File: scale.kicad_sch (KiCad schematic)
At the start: 10 parts, among them J1 Conn_01x02_Pin, J2 Conn_01x04_Pin, J4 Conn_01x05_Pin

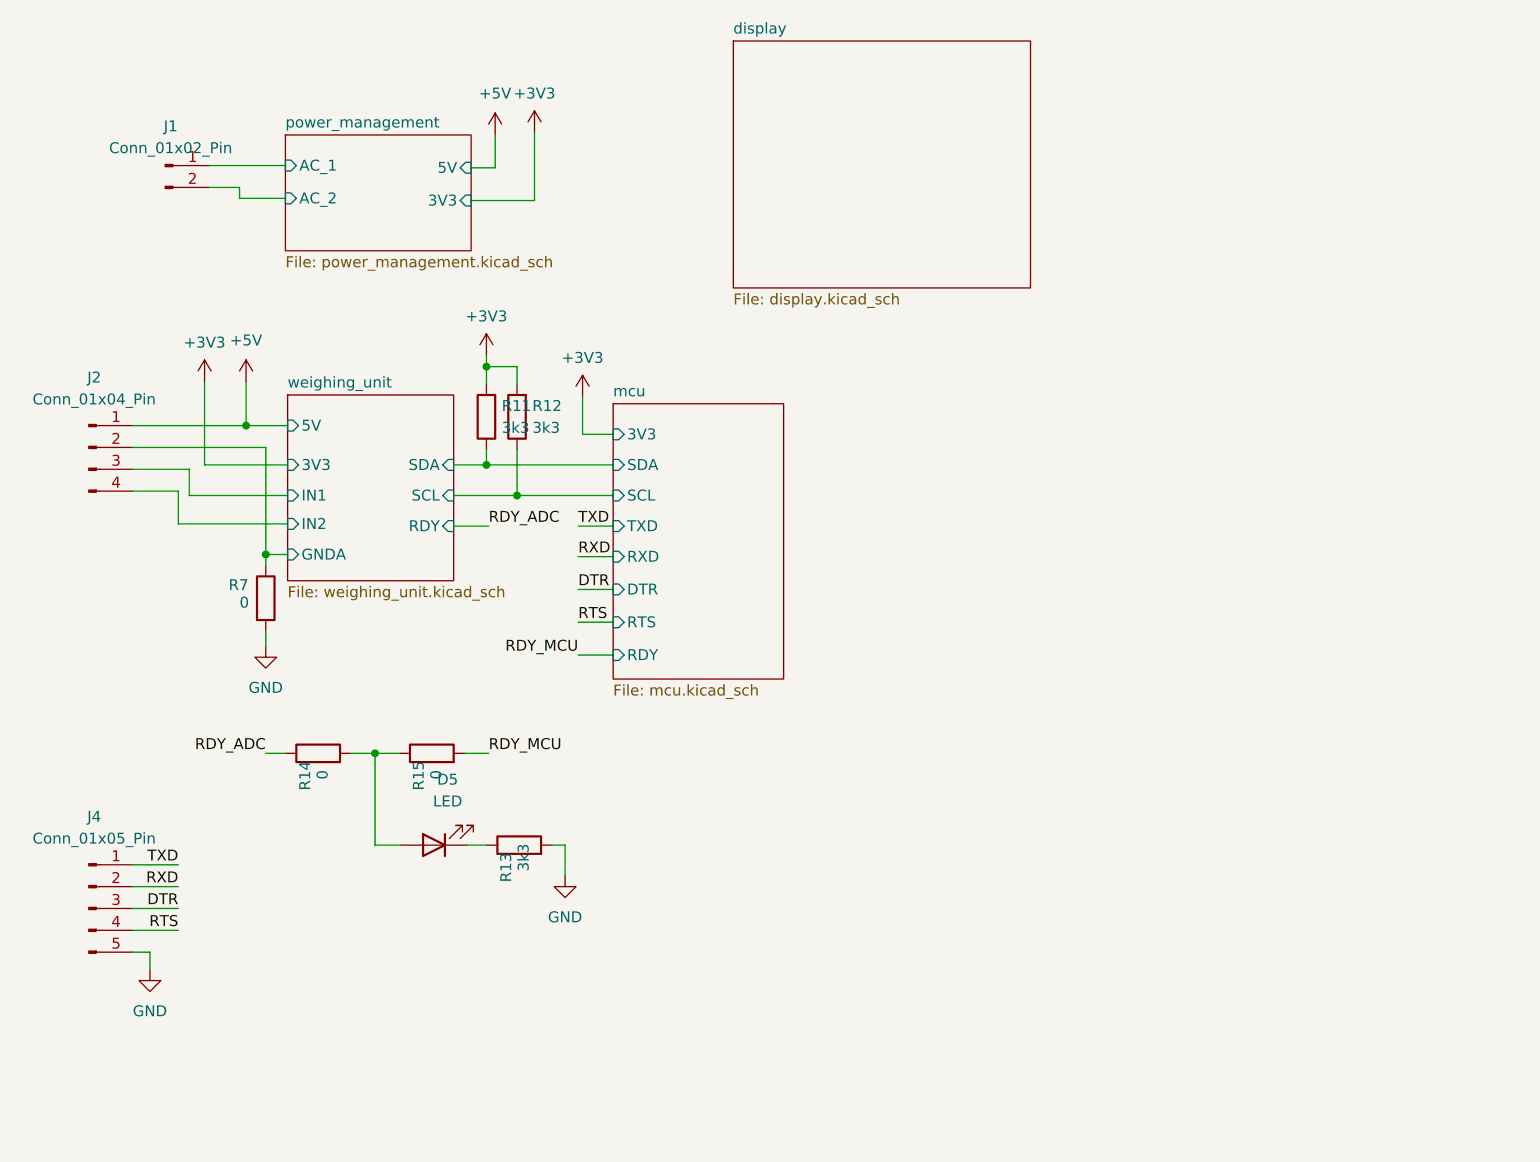
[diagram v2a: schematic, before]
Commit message: add footprint and step
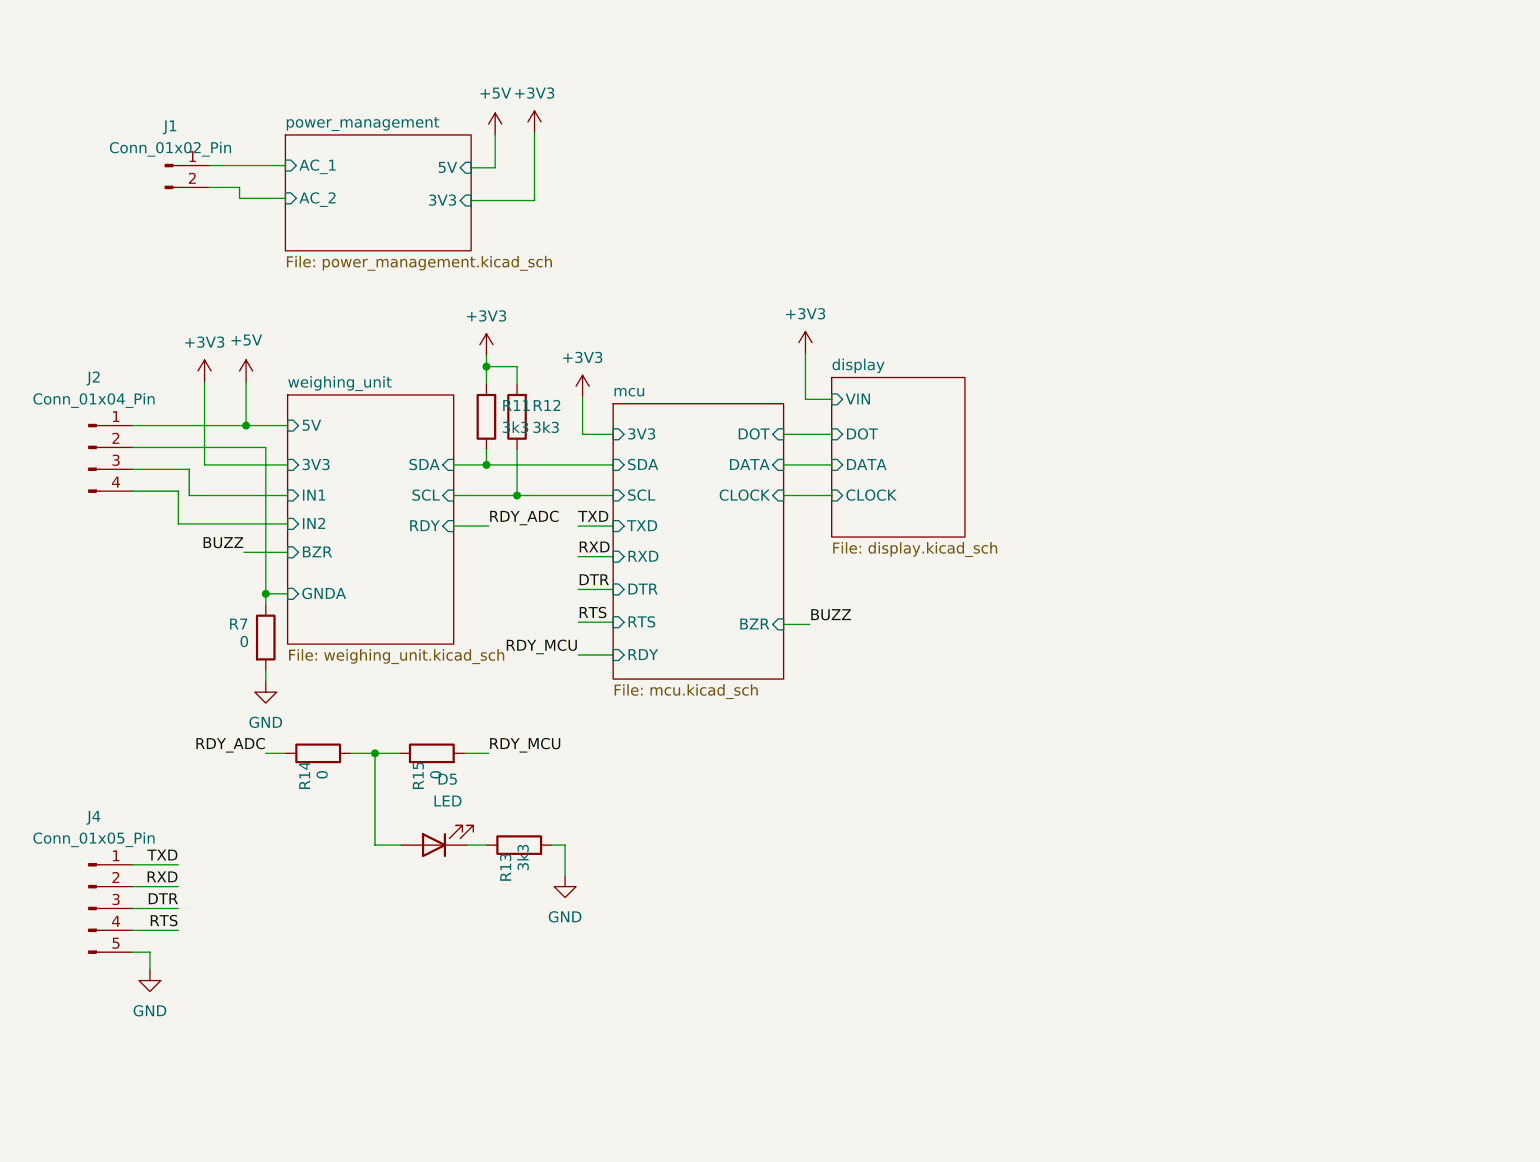
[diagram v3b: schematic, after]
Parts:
- J1: footprint (none) -> BBG:CONN2_284513-2
- J2: footprint (none) -> BBG:JST_S4B-XH-A(LF)(SN)
- J4: footprint (none) -> Connector_PinHeader_2.54mm:PinHeader_1x05_P2.54mm_Vertical
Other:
- sheet display ports: added CLOCK, DATA, DOT, VIN; removed none
- sheet mcu ports: added BZR, CLOCK, DATA, DOT; removed none
- sheet weighing_unit ports: added BZR; removed none
- moved on the sheet: R7
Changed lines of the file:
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@@
   (junction (at 41.402 77.978) (diameter 0) (color 0 0 0 0)
   )
-  (junction (at 43.688 92.964) (diameter 0) (color 0 0 0 0)
-  )
-  (wire (pts (xy 46.228 92.964) (xy 43.688 92.964))
+  (junction (at 43.688 97.536) (diameter 0) (color 0 0 0 0)
+  )
+  (wire (pts (xy 46.228 97.536) (xy 43.688 97.536))
     (stroke (width 0) (type default))
   )
@@
     (stroke (width 0) (type default))
   )
-  (wire (pts (xy 43.688 80.518) (xy 43.688 92.964))
-    (stroke (width 0) (type default))
-  )
   (wire (pts (xy 34.798 83.058) (xy 28.194 83.058))
     (stroke (width 0) (type default))
@@
     (stroke (width 0) (type default))
   )
+  (wire (pts (xy 103.886 78.994) (xy 109.474 78.994))
+    (stroke (width 0) (type default))
+  )
   (wire (pts (xy 36.576 72.898) (xy 36.576 82.55))
     (stroke (width 0) (type default))
@@
     (stroke (width 0) (type default))
   )
+  (wire (pts (xy 103.886 86.106) (xy 109.474 86.106))
+    (stroke (width 0) (type default))
+  )
   (wire (pts (xy 46.228 86.106) (xy 34.798 86.106))
     (stroke (width 0) (type default))
@@
     (stroke (width 0) (type default))
   )
-  (wire (pts (xy 43.688 92.964) (xy 43.688 94.234))
+  (wire (pts (xy 43.688 80.518) (xy 43.688 97.536))
     (stroke (width 0) (type default))
   )
@@
     (stroke (width 0) (type default))
   )
+  (wire (pts (xy 103.886 82.55) (xy 109.474 82.55))
+    (stroke (width 0) (type default))
+  )
   (wire (pts (xy 40.64 50.292) (xy 37.084 50.292))
     (stroke (width 0) (type default))
@@
     (stroke (width 0) (type default))
   )
+  (wire (pts (xy 41.148 92.71) (xy 46.228 92.71))
+    (stroke (width 0) (type default))
+  )
+  (wire (pts (xy 43.688 97.536) (xy 43.688 98.806))
+    (stroke (width 0) (type default))
+  )
   (wire (pts (xy 67.564 48.006) (xy 70.358 48.006))
     (stroke (width 0) (type default))
@@
     (stroke (width 0) (type default))
   )
-  (wire (pts (xy 43.688 101.854) (xy 43.688 103.632))
+  (wire (pts (xy 103.886 101.092) (xy 106.934 101.092))
+    (stroke (width 0) (type default))
+  )
+  (wire (pts (xy 43.688 106.426) (xy 43.688 107.696))
     (stroke (width 0) (type default))
   )
@@
     (stroke (width 0) (type default))
   )
+  (wire (pts (xy 106.426 74.93) (xy 106.426 69.596))
+    (stroke (width 0) (type default))
+  )
   (wire (pts (xy 28.194 129.032) (xy 33.528 129.032))
     (stroke (width 0) (type default))
@@
   )
   (wire (pts (xy 43.688 116.078) (xy 45.974 116.078))
+    (stroke (width 0) (type default))
+  )
+  (wire (pts (xy 109.474 74.93) (xy 106.426 74.93))
     (stroke (width 0) (type default))
   )
@@
     (effects (font (size 1.27 1.27)) (justify left bottom))
   )
+  (label "BUZZ" (at 41.148 92.71 180) (fields_autoplaced)
+    (effects (font (size 1.27 1.27)) (justify right bottom))
+  )
+  (label "BUZZ" (at 106.934 101.092 0) (fields_autoplaced)
+    (effects (font (size 1.27 1.27)) (justify left bottom))
+  )
   (symbol (lib_id "power:+5V") (at 41.402 72.898 0) (unit 1)
     (in_bom yes) (on_board yes) (dnp no) (fields_autoplaced)
@@
       (effects (font (size 1.27 1.27)))
     )
-    (property "Footprint" "" (at 23.114 80.518 0)
+    (property "Footprint" "BBG:JST_S4B-XH-A(LF)(SN)" (at 23.114 80.518 0)
       (effects (font (size 1.27 1.27)) hide)
     )
@@
       (effects (font (size 1.27 1.27)))
     )
-    (property "Footprint" "" (at 32.004 47.752 0)
+    (property "Footprint" "BBG:CONN2_284513-2" (at 32.004 47.752 0)
       (effects (font (size 1.27 1.27)) hide)
     )
@@
     )
   )
-  (symbol (lib_id "power:GND") (at 43.688 103.632 0) (unit 1)
-    (in_bom yes) (on_board yes) (dnp no) (fields_autoplaced)
-    (property "Reference" "#PWR016" (at 43.688 109.982 0)
-      (effects (font (size 1.27 1.27)) hide)
-    )
-    (property "Value" "GND" (at 43.688 108.458 0)
-      (effects (font (size 1.27 1.27)))
-    )
-    (property "Footprint" "" (at 43.688 103.632 0)
-      (effects (font (size 1.27 1.27)) hide)
-    )
-    (property "Datasheet" "" (at 43.688 103.632 0)
+  (symbol (lib_id "power:GND") (at 43.688 107.696 0) (unit 1)
+    (in_bom yes) (on_board yes) (dnp no) (fields_autoplaced)
+    (property "Reference" "#PWR016" (at 43.688 114.046 0)
+      (effects (font (size 1.27 1.27)) hide)
+    )
+    (property "Value" "GND" (at 43.688 112.522 0)
+      (effects (font (size 1.27 1.27)))
+    )
+    (property "Footprint" "" (at 43.688 107.696 0)
+      (effects (font (size 1.27 1.27)) hide)
+    )
+    (property "Datasheet" "" (at 43.688 107.696 0)
       (effects (font (size 1.27 1.27)) hide)
     )
@@
       (effects (font (size 1.27 1.27)))
     )
-    (property "Footprint" "" (at 23.114 134.112 0)
+    (property "Footprint" "Connector_PinHeader_2.54mm:PinHeader_1x05_P2.54mm_Vertical" (at 23.114 134.112 0)
       (effects (font (size 1.27 1.27)) hide)
     )
@@
     )
   )
+  (symbol (lib_id "power:+3V3") (at 106.426 69.596 0) (unit 1)
+    (in_bom yes) (on_board yes) (dnp no) (fields_autoplaced)
+    (property "Reference" "#PWR031" (at 106.426 73.406 0)
+      (effects (font (size 1.27 1.27)) hide)
+    )
+    (property "Value" "+3V3" (at 106.426 65.024 0)
+      (effects (font (size 1.27 1.27)))
+    )
+    (property "Footprint" "" (at 106.426 69.596 0)
+      (effects (font (size 1.27 1.27)) hide)
+    )
+    (property "Datasheet" "" (at 106.426 69.596 0)
+      (effects (font (size 1.27 1.27)) hide)
+    )
+    (pin "1")
+    (instances
+      (project "scale"
+        (path "/8f227bf3-f4cf-485c-a746-8377af835d89"
+          (reference "#PWR031") (unit 1)
+        )
+      )
+    )
+  )
   (symbol (lib_id "Device:R") (at 49.784 116.078 90) (unit 1)
     (in_bom yes) (on_board yes) (dnp no)
@@
     )
   )
-  (symbol (lib_id "Device:R") (at 43.688 98.044 0) (unit 1)
+  (symbol (lib_id "Device:R") (at 43.688 102.616 0) (unit 1)
     (in_bom yes) (on_board yes) (dnp no)
-    (property "Reference" "R7" (at 39.37 96.52 0)
-      (effects (font (size 1.27 1.27)) (justify left))
-    )
-    (property "Value" "0" (at 40.64 98.552 0)
-      (effects (font (size 1.27 1.27)) (justify left))
-    )
-    (property "Footprint" "Resistor_SMD:R_0805_2012Metric" (at 41.91 98.044 90)
-      (effects (font (size 1.27 1.27)) hide)
-    )
-    (property "Datasheet" "~" (at 43.688 98.044 0)
+    (property "Reference" "R7" (at 39.37 101.092 0)
+      (effects (font (size 1.27 1.27)) (justify left))
+    )
+    (property "Value" "0" (at 40.64 103.124 0)
+      (effects (font (size 1.27 1.27)) (justify left))
+    )
+    (property "Footprint" "Resistor_SMD:R_0805_2012Metric" (at 41.91 102.616 90)
+      (effects (font (size 1.27 1.27)) hide)
+    )
+    (property "Datasheet" "~" (at 43.688 102.616 0)
       (effects (font (size 1.27 1.27)) hide)
     )
@@
       (effects (font (size 1.27 1.27)) (justify left))
     )
+    (pin "DOT" input (at 103.886 78.994 0)
+      (effects (font (size 1.27 1.27)) (justify right))
+    )
+    (pin "DATA" input (at 103.886 82.55 0)
+      (effects (font (size 1.27 1.27)) (justify right))
+    )
+    (pin "CLOCK" input (at 103.886 86.106 0)
+      (effects (font (size 1.27 1.27)) (justify right))
+    )
+    (pin "BZR" input (at 103.886 101.092 0)
+      (effects (font (size 1.27 1.27)) (justify right))
+    )
     (instances
       (project "scale"
@@
     )
   )
-  (sheet (at 46.228 74.422) (size 19.304 21.59) (fields_autoplaced)
+  (sheet (at 46.228 74.422) (size 19.304 28.956) (fields_autoplaced)
     (stroke (width 0.1524) (type solid))
     (fill (color 0 0 0 0.0000))
@@
       (effects (font (size 1.27 1.27)) (justify left bottom))
     )
-    (property "Sheetfile" "weighing_unit.kicad_sch" (at 46.228 96.5966 0)
+    (property "Sheetfile" "weighing_unit.kicad_sch" (at 46.228 103.9626 0)
       (effects (font (size 1.27 1.27)) (justify left top))
     )
@@
       (effects (font (size 1.27 1.27)) (justify left))
     )
-    (pin "GNDA" input (at 46.228 92.964 180)
+    (pin "GNDA" input (at 46.228 97.536 180)
       (effects (font (size 1.27 1.27)) (justify left))
     )
@@
     (pin "SDA" input (at 65.532 82.55 0)
       (effects (font (size 1.27 1.27)) (justify right))
+    )
+    (pin "BZR" input (at 46.228 92.71 180)
+      (effects (font (size 1.27 1.27)) (justify left))
     )
     (instances
@@
     )
   )
-  (sheet (at 98.044 33.274) (size 34.544 28.702) (fields_autoplaced)
+  (sheet (at 109.474 72.39) (size 15.494 18.542) (fields_autoplaced)
     (stroke (width 0.1524) (type solid))
     (fill (color 0 0 0 0.0000))
-    (property "Sheetname" "display" (at 98.044 32.5624 0)
+    (property "Sheetname" "display" (at 109.474 71.6784 0)
       (effects (font (size 1.27 1.27)) (justify left bottom))
     )
-    (property "Sheetfile" "display.kicad_sch" (at 98.044 62.5606 0)
+    (property "Sheetfile" "display.kicad_sch" (at 109.474 91.5166 0)
       (effects (font (size 1.27 1.27)) (justify left top))
     )
-    (instances
+    (pin "VIN" input (at 109.474 74.93 180)
+      (effects (font (size 1.27 1.27)) (justify left))
+    )
+    (pin "DATA" input (at 109.474 82.55 180)
+      (effects (font (size 1.27 1.27)) (justify left))
+    )
+    (pin "DOT" input (at 109.474 78.994 180)
+      (effects (font (size 1.27 1.27)) (justify left))
+    )
+    (pin "CLOCK" input (at 109.474 86.106 180)
+      (effects (font (size 1.27 1.27)) (justify left))
+    )
+    (instances

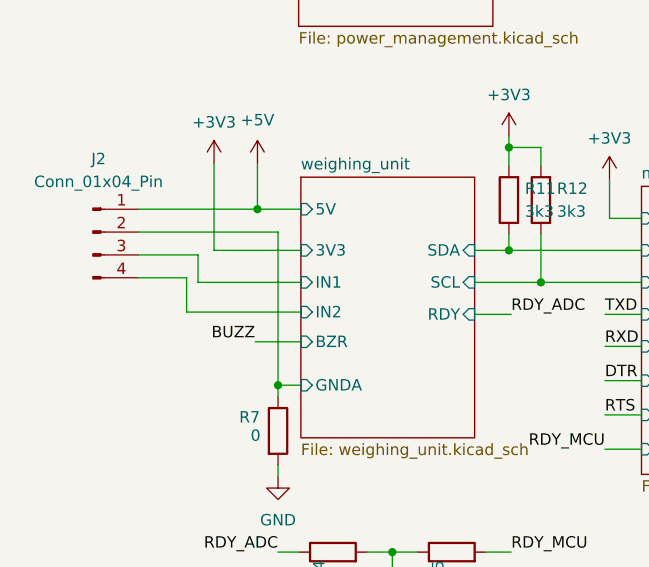
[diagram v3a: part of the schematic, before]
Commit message: routing some signals: I2C, EN, IO0, BUZZ
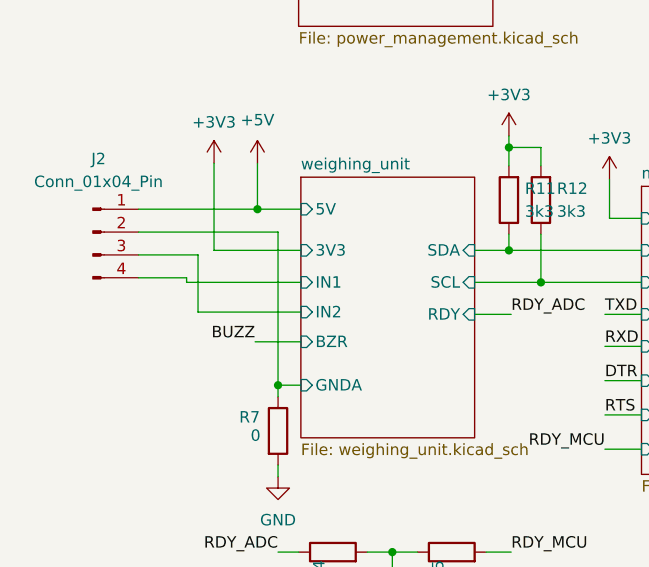
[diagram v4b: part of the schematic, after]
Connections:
- net weighing_unit/IN1: now also J2.4 (Pin_4); no longer J2.3 (Pin_3)
- net weighing_unit/IN2: now also J2.3 (Pin_3); no longer J2.4 (Pin_4)
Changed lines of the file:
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@@
+    (stroke (width 0) (type default))
+  )
+  (wire (pts (xy 46.228 89.408) (xy 34.798 89.408))
     (stroke (width 0) (type default))
   )
@@
   )
   (wire (pts (xy 70.358 48.006) (xy 70.358 44.196))
-    (stroke (width 0) (type default))
-  )
-  (wire (pts (xy 33.528 89.408) (xy 46.228 89.408))
     (stroke (width 0) (type default))
   )
@@
     (stroke (width 0) (type default))
   )
+  (wire (pts (xy 33.528 86.106) (xy 46.228 86.106))
+    (stroke (width 0) (type default))
+  )
   (wire (pts (xy 28.194 134.112) (xy 33.528 134.112))
     (stroke (width 0) (type default))
@@
   )
   (wire (pts (xy 103.886 86.106) (xy 109.474 86.106))
-    (stroke (width 0) (type default))
-  )
-  (wire (pts (xy 46.228 86.106) (xy 34.798 86.106))
     (stroke (width 0) (type default))
   )
@@
     (stroke (width 0) (type default))
   )
-  (wire (pts (xy 33.528 85.598) (xy 33.528 89.408))
+  (wire (pts (xy 33.528 85.598) (xy 33.528 86.106))
     (stroke (width 0) (type default))
   )
@@
     (stroke (width 0) (type default))
   )
+  (wire (pts (xy 34.798 89.408) (xy 34.798 83.058))
+    (stroke (width 0) (type default))
+  )
   (wire (pts (xy 106.426 74.93) (xy 106.426 69.596))
     (stroke (width 0) (type default))
@@
     (stroke (width 0) (type default))
   )
-  (wire (pts (xy 34.798 86.106) (xy 34.798 83.058))
-    (stroke (width 0) (type default))
-  )

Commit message: start routing
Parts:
- removed R14, R15: 0, Resistor_SMD:R_0402_1005Metric, symbol Device:R
- added J6: Conn_01x03_Pin, BBG:CONN_S3B-XH-ALFSN_JST, symbol Connector:Conn_01x03_Pin
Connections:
- net GND: now also R13.1, J6.3 (Pin_3); no longer R13.2
- net weighing_unit/RDY: now reaches D5.2 (A)
- net at D5.1 (K): now also R13.2; no longer R13.1
- new net BUT0: J6.1 (Pin_1)
- new net BUT1: J6.2 (Pin_2)
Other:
- sheet mcu ports: added BUT0, BUT1; removed RDY
- moved on the sheet: R13
